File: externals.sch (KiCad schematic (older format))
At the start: 78 parts, among them J1 SWD, J2 RC522_Header, J3 Screw_Terminal_1x02, P2 VolDown, P3 Prev, P4 Play, P5 Next, P6 VolUp, P7 CONN_02X10, Q1 BSS138

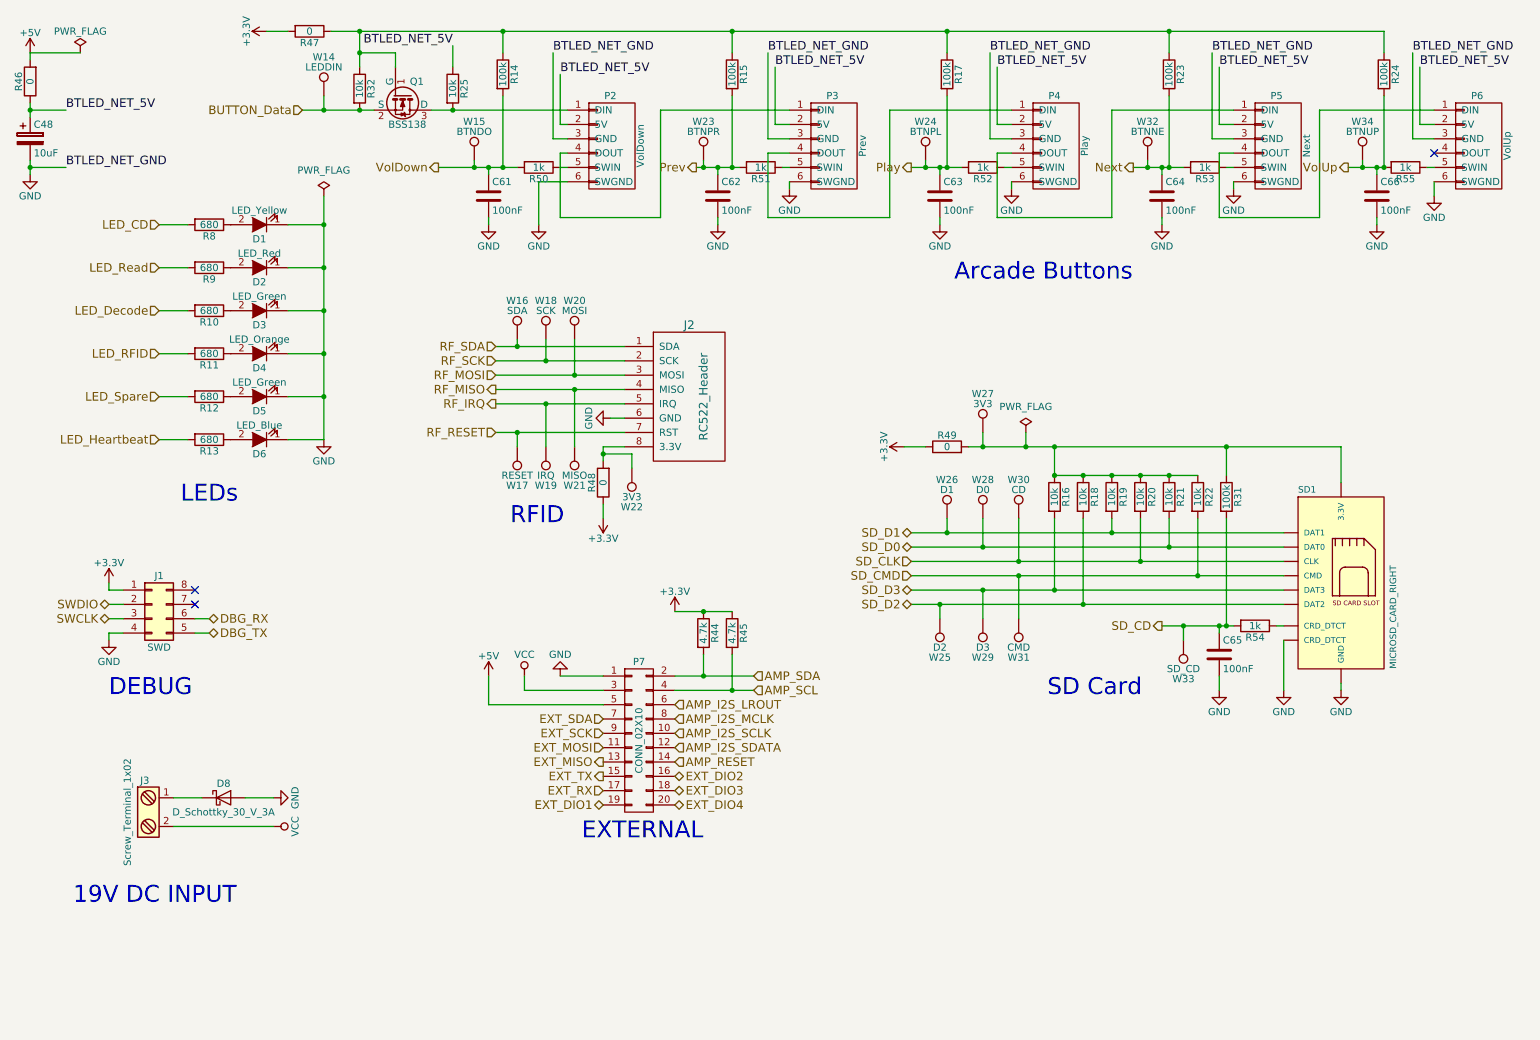
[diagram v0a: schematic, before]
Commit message: Changed butten connectors
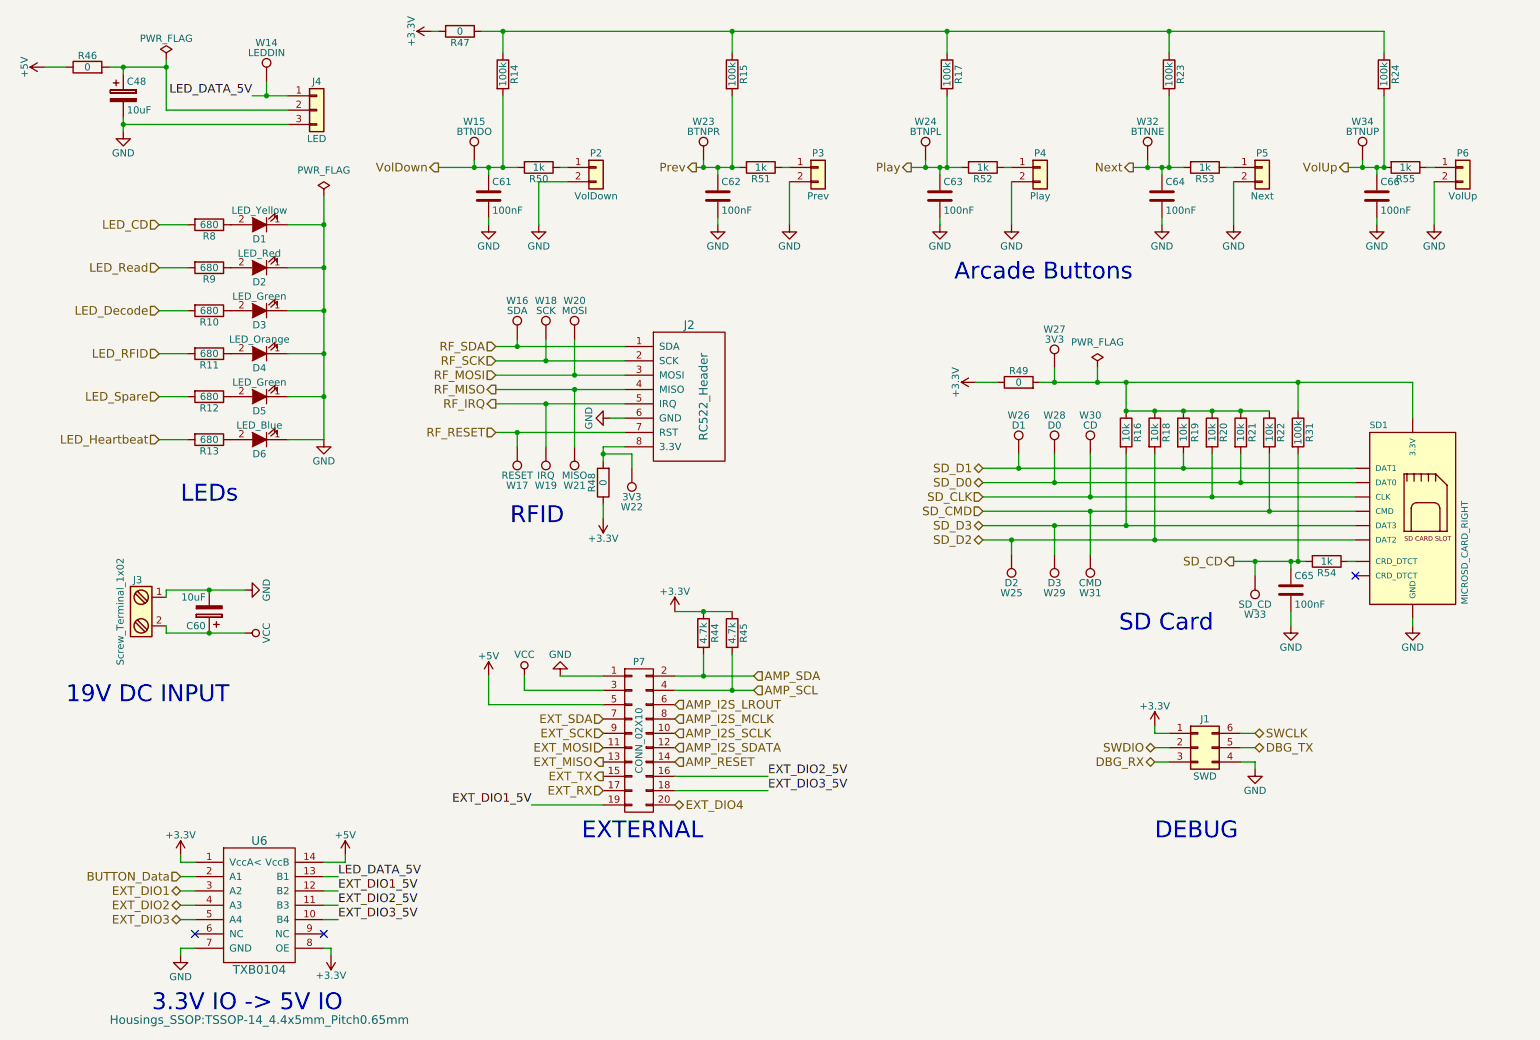
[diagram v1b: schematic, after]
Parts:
- removed D8: D_Schottky_30_V_3A, Diodes_SMD:SMB_Standard, symbol D_Schottky
- removed J1: SWD, Pin_Headers:Pin_Header_Straight_2x04, symbol Conn_02x04_Counter_Clockwise
- removed P2: VolDown, Pin_Headers:Pin_Header_Straight_1x06, symbol BUTTON-RESCUE-tmb_musicplayer
- removed P3: Prev, Pin_Headers:Pin_Header_Straight_1x06, symbol BUTTON-RESCUE-tmb_musicplayer
- removed P4: Play, Pin_Headers:Pin_Header_Straight_1x06, symbol BUTTON-RESCUE-tmb_musicplayer
- removed P5: Next, Pin_Headers:Pin_Header_Straight_1x06, symbol BUTTON-RESCUE-tmb_musicplayer
- removed P6: VolUp, Pin_Headers:Pin_Header_Straight_1x06, symbol BUTTON-RESCUE-tmb_musicplayer
- removed Q1: BSS138, TO_SOT_Packages_SMD:SOT-23, symbol BSS138-RESCUE-tmb_musicplayer
- removed R25, R32: 10k, Resistors_SMD:R_0603, symbol R
- added C60: 10uF, Capacitors_THT:C_Radial_D13_L21_P5, symbol CP
- added J1: SWD, Pin_Headers:Pin_Header_Straight_2x03, symbol Conn_02x03_Counter_Clockwise
- added J4: LED, Connectors_JST:JST_XH_B03B-XH-A_03x2.50mm_Straight, symbol Conn_01x03
- added P2: VolDown, Connectors_JST:JST_XH_B02B-XH-A_02x2.50mm_Straight, symbol Conn_01x02
- added P3: Prev, Connectors_JST:JST_XH_B02B-XH-A_02x2.50mm_Straight, symbol Conn_01x02
- added P4: Play, Connectors_JST:JST_XH_B02B-XH-A_02x2.50mm_Straight, symbol Conn_01x02
- added P5: Next, Connectors_JST:JST_XH_B02B-XH-A_02x2.50mm_Straight, symbol Conn_01x02
- added P6: VolUp, Connectors_JST:JST_XH_B02B-XH-A_02x2.50mm_Straight, symbol Conn_01x02
- added U6: TXB0104, Housings_SSOP:TSSOP-14_4.4x5mm_Pitch0.65mm, symbol TXB0104
- SD1: footprint MF_Connectors_MF-MICROSD -> jfi:MF_Connectors-MF-MICROSD
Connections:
- net +3V3: now also J1.1 (Pin_1), U6.1 (VccA<), U6.8 (OE)
- net +5V: now also R46.1, U6.14 (VccB); no longer R46.2
- net BUTTON_Data: now also U6.2 (A1); no longer W14.1
- net DBG_RX: now also J1.3 (Pin_3)
- net DBG_TX: now also J1.5 (Pin_5)
- net EXT_DIO1: now also U6.3 (A2); no longer P7.19 (P19)
- net EXT_DIO2: now also U6.4 (A3); no longer P7.16 (P16)
- net EXT_DIO3: now also U6.5 (A4); no longer P7.18 (P18)
- net GND: now also J3.1, C60.2, J1.4 (Pin_4), J4.3 (Pin_3), P2.2 (Pin_2), P3.2 (Pin_2), P4.2 (Pin_2), P5.2 (Pin_2), P6.2 (Pin_2), U6.7 (GND); no longer SD1.10 (CRD_DTCT)
- net SWCLK: now also J1.6 (Pin_6)
- net SWDIO: now also J1.2 (Pin_2)
- net VCC: now also C60.1
- net at R50.1: now also P2.1 (Pin_1)
- net at R51.1: now also P3.1 (Pin_1)
- net at R52.1: now also P4.1 (Pin_1)
- net at R53.1: now also P5.1 (Pin_1)
- net at R55.1: now also P6.1 (Pin_1)
- net BTLED_NET_5V: no longer names the net of C48.1
- net BTLED_NET_5V: now also R46.2, J4.2 (Pin_2); no longer R46.1
- new net EXT_DIO1_5V: P7.19 (P19), U6.12 (B2)
- new net EXT_DIO2_5V: P7.16 (P16), U6.11 (B3)
- new net EXT_DIO3_5V: P7.18 (P18), U6.10 (B4)
- new net LED_DATA_5V: J4.1 (Pin_1), U6.13 (B1), W14.1
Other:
- note added: "3.3V IO -> 5V IO"
- moved on the sheet: C48, C65, J3, R16, R18, R19, R20, R21, R22, R31, R46, R47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
